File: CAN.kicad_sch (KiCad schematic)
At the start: 32 parts, among them U7 MCP2515-xST, U8 SN65HVD230, Y1 16MHz

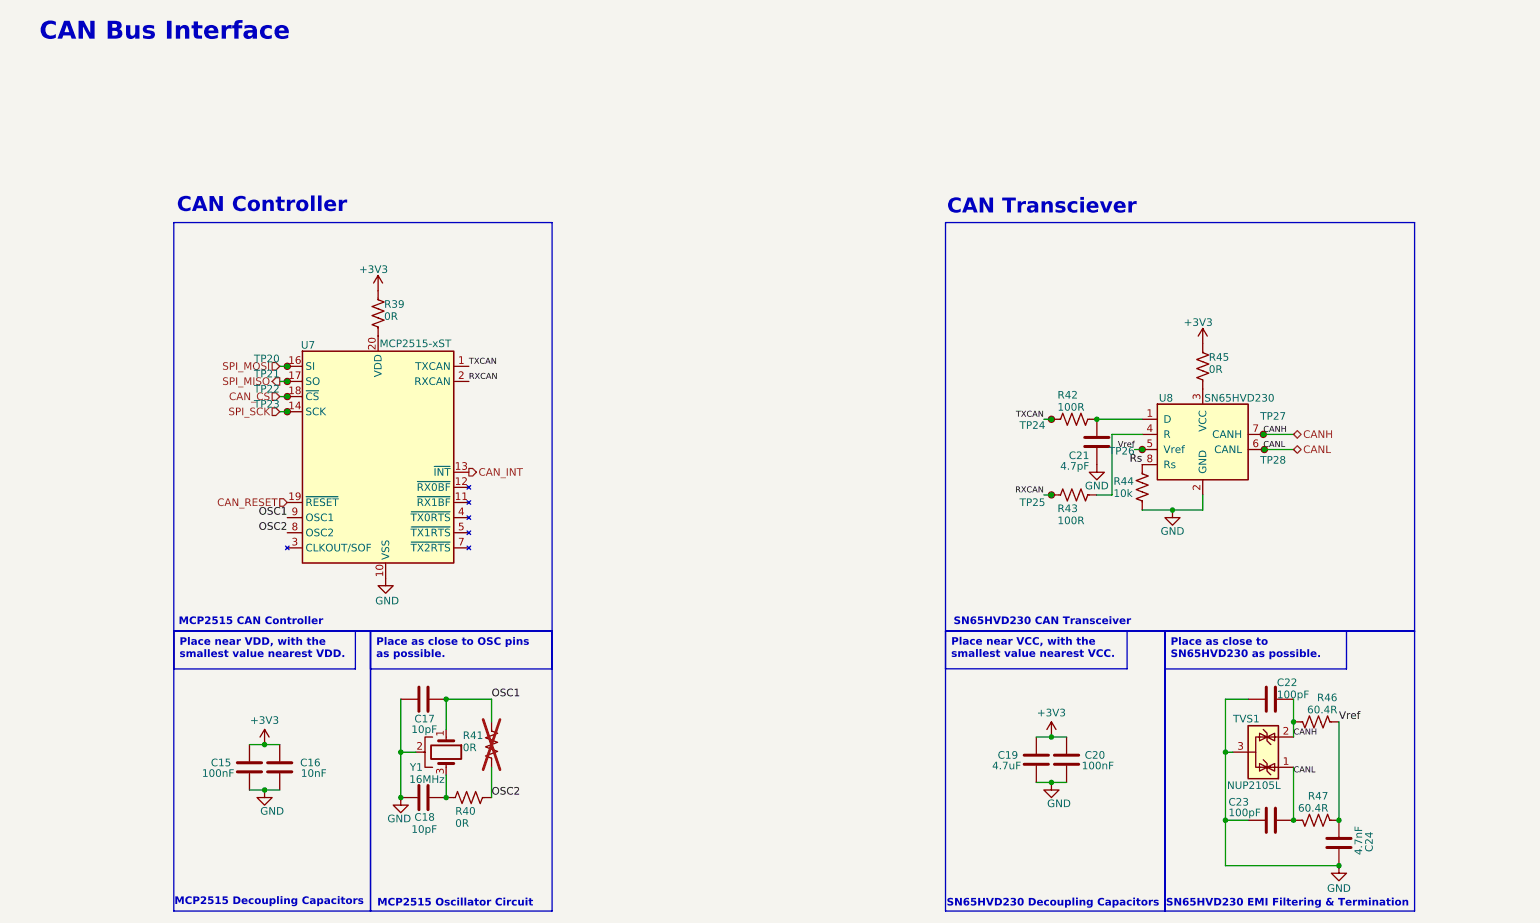
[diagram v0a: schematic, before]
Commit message: Added labels and schematic PDF among other progress
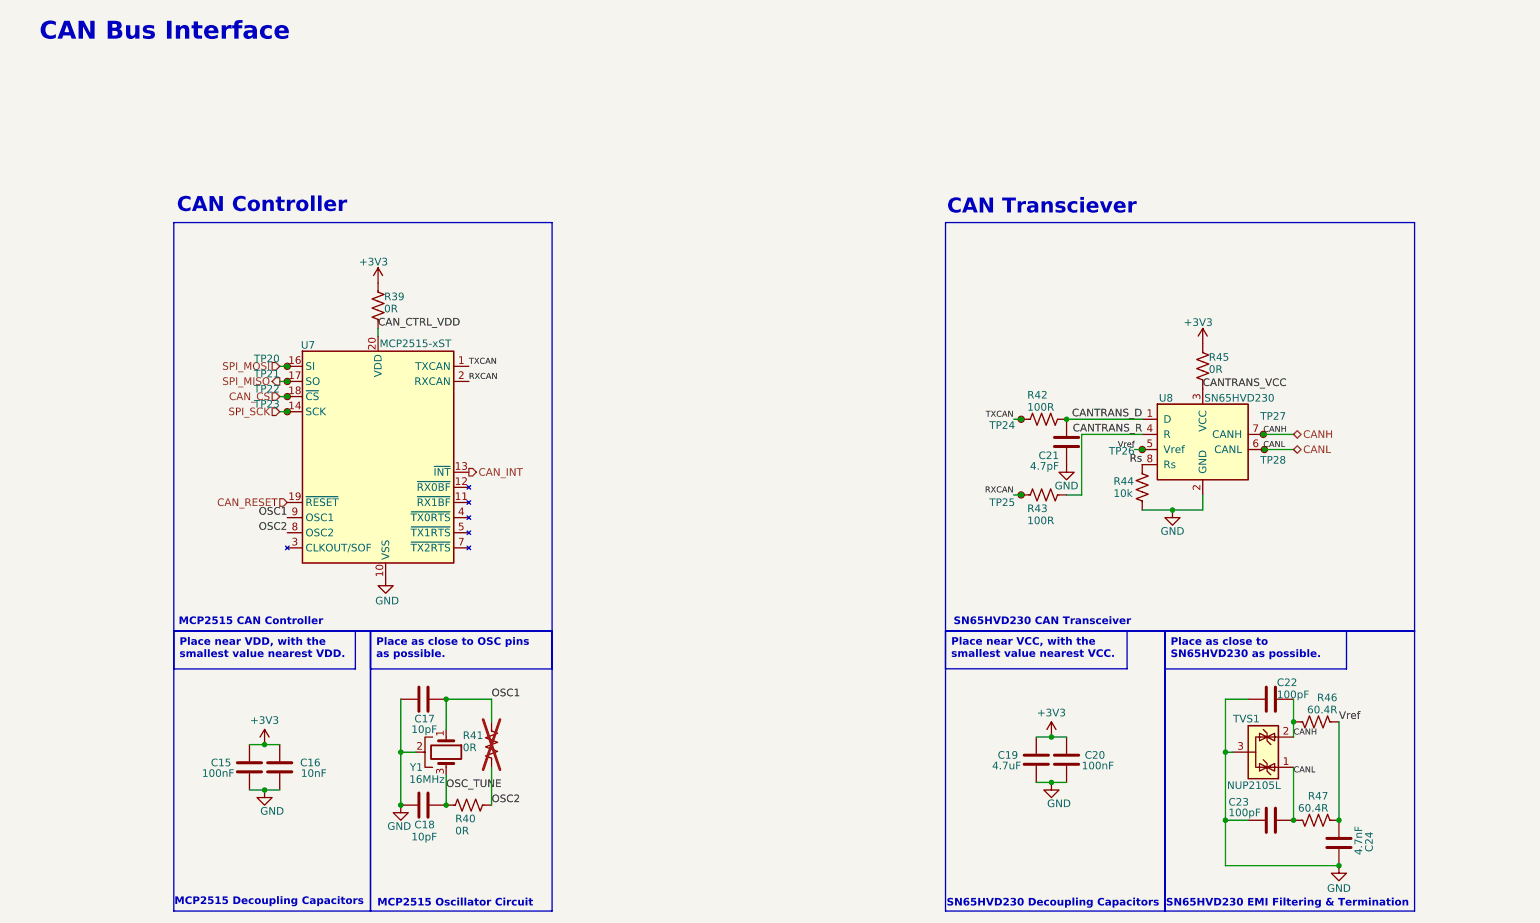
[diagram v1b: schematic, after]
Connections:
- net OSC_TUNE: now reaches C18.2, R40.1, Y1.3
- net CANTRANS_D: now reaches C21.1, R42.2, U8.1 (D)
- net CANTRANS_VCC: now reaches R45.2, U8.3 (VCC)
- net CANTRANS_R: now reaches R43.1, U8.4 (R)
- net CAN_CTRL_VDD: now reaches R39.2, U7.20 (VDD)
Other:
- moved on the sheet: C18, C21, R39, R40, R42, R43, TP24, TP25

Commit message: Added testpoints
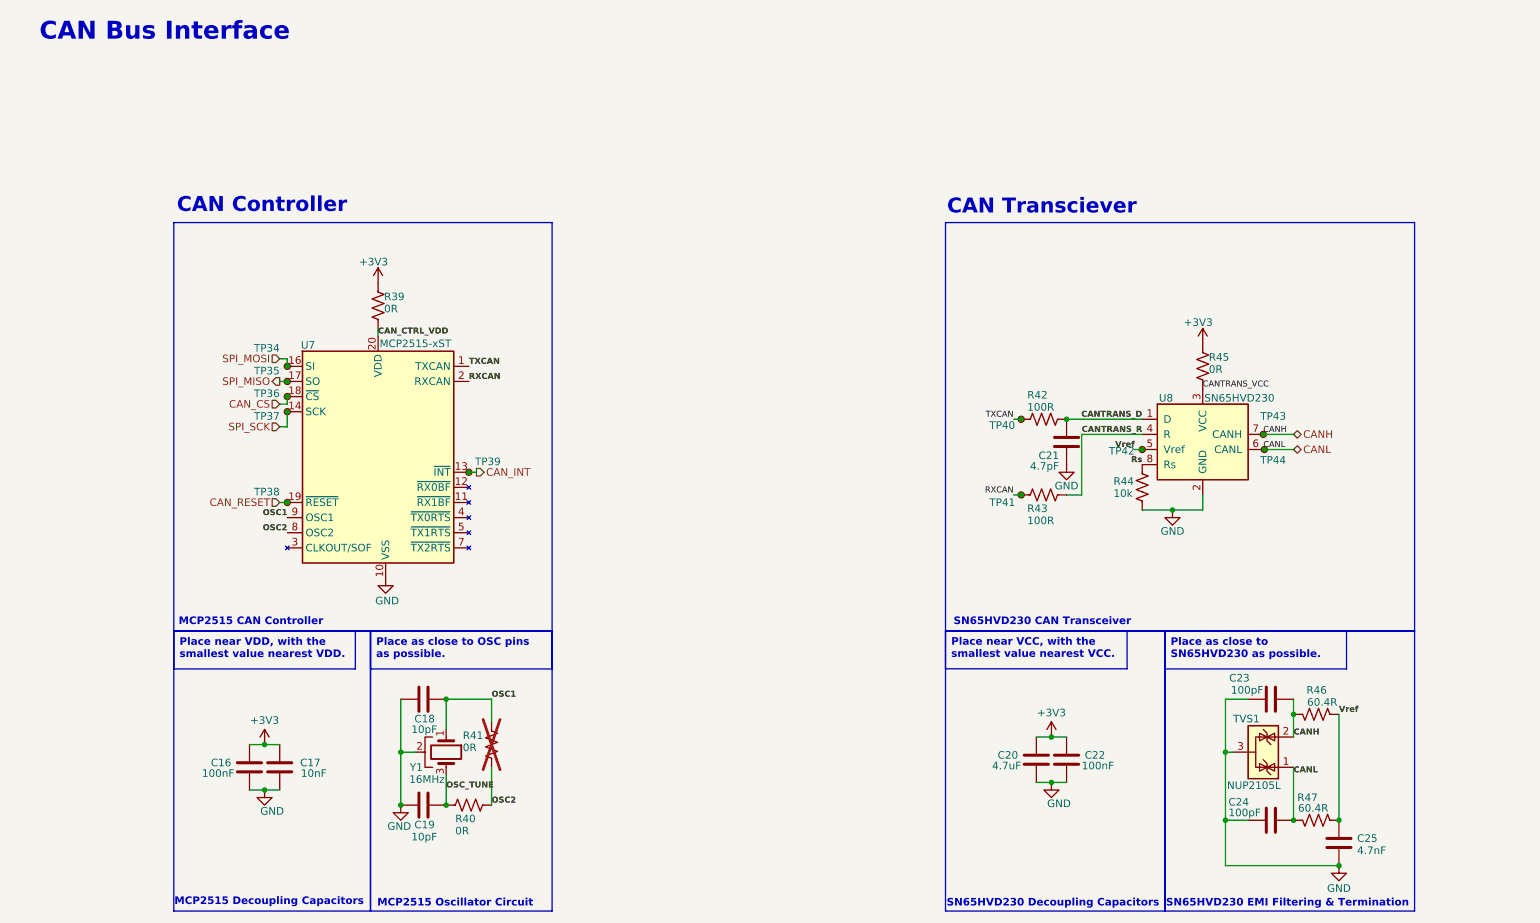
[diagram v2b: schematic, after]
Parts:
- added TP38: CAN_RESET, symbol Connector:TestPoint_Small
- added TP39: CAN_INT, symbol Connector:TestPoint_Small
- renumbered C15 to C16, C16 to C17, C17 to C18, C18 to C19, C19 to C20, C20 to C22, C22 to C23, C23 to C24, C24 to C25, TP20 to TP34, TP21 to TP35, TP22 to TP36, TP23 to TP37, TP24 to TP40, TP25 to TP41, TP26 to TP42, TP27 to TP43, TP28 to TP44
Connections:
- net CANH: now also C23.2; no longer C23.1
- net CAN_INT: now also TP39.1
- net CAN_RESET: now also TP38.1
- net GND: now also C23.1; no longer C23.2
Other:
- moved on the sheet: C23, R46

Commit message: Partially assigned netclasses WIP
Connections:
- net CANTRANS_VCC renamed CAN_TRANS_VCC
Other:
- moved on the sheet: R45
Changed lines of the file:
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@@
 	(wire
 		(pts
+			(xy 69.85 57.15) (xy 69.85 58.42)
+		)
+		(stroke
+			(width 0)
+			(type default)
+		)
+	)
+	(wire
+		(pts
 			(xy 212.09 156.21) (xy 231.14 156.21)
 		)
@@
 	(wire
 		(pts
+			(xy 86.36 74.93) (xy 85.09 74.93)
+		)
+		(stroke
+			(width 0)
+			(type default)
+		)
+	)
+	(wire
+		(pts
 			(xy 53.34 143.51) (xy 50.8 143.51)
 		)
@@
 	(wire
 		(pts
+			(xy 86.36 72.39) (xy 85.09 72.39)
+		)
+		(stroke
+			(width 0)
+			(type default)
+		)
+	)
+	(wire
+		(pts
 			(xy 54.61 78.74) (xy 54.61 77.47)
 		)
@@
 	(wire
 		(pts
+			(xy 208.28 66.04) (xy 208.28 67.31)
+		)
+		(stroke
+			(width 0)
+			(type default)
+		)
+	)
+	(wire
+		(pts
 			(xy 53.34 74.93) (xy 54.61 74.93)
 		)
@@
 	(wire
 		(pts
+			(xy 208.28 74.93) (xy 208.28 76.2)
+		)
+		(stroke
+			(width 0)
+			(type default)
+		)
+	)
+	(wire
+		(pts
 			(xy 50.8 143.51) (xy 48.26 143.51)
 		)
@@
 		)
 	)
-	(label "CANTRANS_VCC"
+	(label "CAN_TRANS_VCC"
 		(at 208.28 76.2 0)
 		(effects
@@
 	)
 	(label "TXCAN"
-		(at 85.09 72.39 0)
+		(at 86.36 72.39 0)
 		(effects
 			(font
@@
 	)
 	(label "RXCAN"
-		(at 85.09 74.93 0)
+		(at 86.36 74.93 0)
 		(effects
 			(font
@@
 	(symbol
 		(lib_id "power:+3V3")
-		(at 208.28 68.58 0)
+		(at 208.28 66.04 0)
 		(unit 1)
 		(body_style 1)
@@
 		(dnp no)
 		(property "Reference" "#PWR052"
-			(at 208.28 72.39 0)
+			(at 208.28 69.85 0)
 			(hide yes)
 			(show_name no)
@@
 		)
 		(property "Value" "+3V3"
-			(at 207.518 65.024 0)
+			(at 207.518 62.484 0)
 			(show_name no)
 			(do_not_autoplace no)
@@
 		)
 		(property "Footprint" ""
-			(at 208.28 68.58 0)
+			(at 208.28 66.04 0)
 			(hide yes)
 			(show_name no)
@@
 		)
 		(property "Datasheet" ""
-			(at 208.28 68.58 0)
+			(at 208.28 66.04 0)
 			(hide yes)
 			(show_name no)
@@
 		)
 		(property "Description" "Power symbol creates a global label with name \"+3V3\""
-			(at 208.28 68.58 0)
+			(at 208.28 66.04 0)
 			(hide yes)
 			(show_name no)
@@
 	(symbol
 		(lib_id "power:+3V3")
-		(at 69.85 58.42 0)
+		(at 69.85 57.15 0)
 		(unit 1)
 		(body_style 1)
@@
 		(dnp no)
 		(property "Reference" "#PWR045"
-			(at 69.85 62.23 0)
+			(at 69.85 60.96 0)
 			(hide yes)
 			(show_name no)
@@
 		)
 		(property "Value" "+3V3"
-			(at 69.088 54.864 0)
+			(at 69.088 53.594 0)
 			(show_name no)
 			(do_not_autoplace no)
@@
 		)
 		(property "Footprint" ""
-			(at 69.85 58.42 0)
+			(at 69.85 57.15 0)
 			(hide yes)
 			(show_name no)
@@
 		)
 		(property "Datasheet" ""
-			(at 69.85 58.42 0)
+			(at 69.85 57.15 0)
 			(hide yes)
 			(show_name no)
@@
 		)
 		(property "Description" "Power symbol creates a global label with name \"+3V3\""
-			(at 69.85 58.42 0)
+			(at 69.85 57.15 0)
 			(hide yes)
 			(show_name no)
@@
 	(symbol
 		(lib_id "Device:R_US")
-		(at 208.28 72.39 0)
+		(at 208.28 71.12 0)
 		(unit 1)
 		(body_style 1)
@@
 		(dnp no)
 		(property "Reference" "R45"
-			(at 209.296 70.866 0)
+			(at 209.296 69.596 0)
 			(show_name no)
 			(do_not_autoplace no)
@@
 		)
 		(property "Value" "0R"
-			(at 209.296 72.898 0)
+			(at 209.296 71.628 0)
 			(show_name no)
 			(do_not_autoplace no)
@@
 		)
 		(property "Footprint" "Resistor_SMD:R_0805_2012Metric"
-			(at 209.296 72.644 90)
+			(at 209.296 71.374 90)
 			(hide yes)
 			(show_name no)
@@
 		)
 		(property "Datasheet" ""
-			(at 208.28 72.39 0)
+			(at 208.28 71.12 0)
 			(hide yes)
 			(show_name no)
@@
 		)
 		(property "Description" "Resistor, US symbol"
-			(at 208.28 72.39 0)
+			(at 208.28 71.12 0)
 			(hide yes)
 			(show_name no)
@@
 		)
 		(property "MFR#" ""
-			(at 208.28 72.39 0)
+			(at 208.28 71.12 0)
 			(hide yes)
 			(show_name no)
@@
 		)
 		(property "Package" "0805"
-			(at 208.28 72.39 0)
+			(at 208.28 71.12 0)
 			(hide yes)
 			(show_name no)
@@
 		)
 		(property "LCSC#" "C54921246"
-			(at 208.28 72.39 0)
+			(at 208.28 71.12 0)
 			(hide yes)
 			(show_name no)

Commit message: Configured Varients
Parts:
- renumbered R39 to R40, R40 to R41, R41 to R42, R42 to R43, R43 to R44, R44 to R45, R45 to R46, R46 to R47, R47 to R48
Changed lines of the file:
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@@
 					(reference "C20")
 					(unit 1)
+					(variant
+						(name "5v Dumb")
+						(dnp yes)
+					)
 				)
 			)
@@
 		(in_pos_files yes)
 		(dnp no)
-		(property "Reference" "R44"
+		(property "Reference" "R45"
 			(at 193.294 91.694 0)
 			(show_name no)
@@
 			(project "power_module"
 				(path "/33e2b92e-f705-4be7-96f4-57092b8ec1ea/2c777b8c-fce7-4c8f-b22a-e5c1ebb4dbeb"
-					(reference "R44")
+					(reference "R45")
 					(unit 1)
+					(variant
+						(name "5v Dumb")
+						(dnp yes)
+					)
 				)
 			)
@@
 					(reference "C19")
 					(unit 1)
+					(variant
+						(name "5v Dumb")
+						(dnp yes)
+					)
 				)
 			)
@@
 					(reference "C25")
 					(unit 1)
+					(variant
+						(name "5v Dumb")
+						(dnp yes)
+					)
 				)
 			)
@@
 					(reference "U8")
 					(unit 1)
+					(variant
+						(name "5v Dumb")
+						(dnp yes)
+					)
 				)
 			)
@@
 					(reference "C22")
 					(unit 1)
+					(variant
+						(name "5v Dumb")
+						(dnp yes)
+					)
 				)
 			)
@@
 					(reference "Y1")
 					(unit 1)
+					(variant
+						(name "5v Dumb")
+						(dnp yes)
+					)
 				)
 			)
@@
 					(reference "C17")
 					(unit 1)
+					(variant
+						(name "5v Dumb")
+						(dnp yes)
+					)
 				)
 			)
@@
 		(in_pos_files yes)
 		(dnp no)
-		(property "Reference" "R47"
+		(property "Reference" "R48"
 			(at 227.584 144.78 90)
 			(show_name no)
@@
 			(project "power_module"
 				(path "/33e2b92e-f705-4be7-96f4-57092b8ec1ea/2c777b8c-fce7-4c8f-b22a-e5c1ebb4dbeb"
-					(reference "R47")
+					(reference "R48")
 					(unit 1)
+					(variant
+						(name "5v Dumb")
+						(dnp yes)
+					)
 				)
 			)
@@
 		(in_pos_files yes)
 		(dnp yes)
-		(property "Reference" "R41"
+		(property "Reference" "R42"
 			(at 84.074 134.366 0)
 			(show_name no)
@@
 			(project "power_module"
 				(path "/33e2b92e-f705-4be7-96f4-57092b8ec1ea/2c777b8c-fce7-4c8f-b22a-e5c1ebb4dbeb"
-					(reference "R41")
+					(reference "R42")
 					(unit 1)
 				)
@@
 					(reference "C24")
 					(unit 1)
+					(variant
+						(name "5v Dumb")
+						(dnp yes)
+					)
 				)
 			)
@@
 		(in_pos_files yes)
 		(dnp no)
-		(property "Reference" "R42"
+		(property "Reference" "R43"
 			(at 178.816 77.216 90)
 			(show_name no)
@@
 			(project "power_module"
 				(path "/33e2b92e-f705-4be7-96f4-57092b8ec1ea/2c777b8c-fce7-4c8f-b22a-e5c1ebb4dbeb"
-					(reference "R42")
+					(reference "R43")
 					(unit 1)
+					(variant
+						(name "5v Dumb")
+						(dnp yes)
+					)
 				)
 			)
@@
 		(in_pos_files yes)
 		(dnp no)
-		(property "Reference" "R45"
+		(property "Reference" "R46"
 			(at 209.296 69.596 0)
 			(show_name no)
@@
 			(project "power_module"
 				(path "/33e2b92e-f705-4be7-96f4-57092b8ec1ea/2c777b8c-fce7-4c8f-b22a-e5c1ebb4dbeb"
-					(reference "R45")
+					(reference "R46")
 					(unit 1)
+					(variant
+						(name "5v Dumb")
+						(dnp yes)
+					)
 				)
 			)
@@
 					(reference "C21")
 					(unit 1)
+					(variant
+						(name "5v Dumb")
+						(dnp yes)
+					)
 				)
 			)
@@
 		(in_pos_files yes)
 		(dnp no)
-		(property "Reference" "R40"
+		(property "Reference" "R41"
 			(at 82.804 148.336 90)
 			(show_name no)
@@
 			(project "power_module"
 				(path "/33e2b92e-f705-4be7-96f4-57092b8ec1ea/2c777b8c-fce7-4c8f-b22a-e5c1ebb4dbeb"
-					(reference "R40")
+					(reference "R41")
 					(unit 1)
+					(variant
+						(name "5v Dumb")
+						(dnp yes)
+					)
 				)
 			)
@@
 					(reference "C16")
 					(unit 1)
+					(variant
+						(name "5v Dumb")
+						(dnp yes)
+					)
 				)
 			)
@@
 		(in_pos_files yes)
 		(dnp no)
-		(property "Reference" "R39"
+		(property "Reference" "R40"
 			(at 70.866 60.706 0)
 			(show_name no)
@@
 			(project "power_module"
 				(path "/33e2b92e-f705-4be7-96f4-57092b8ec1ea/2c777b8c-fce7-4c8f-b22a-e5c1ebb4dbeb"
-					(reference "R39")
+					(reference "R40")
 					(unit 1)
+					(variant
+						(name "5v Dumb")
+						(dnp yes)
+					)
 				)
 			)
@@
 					(reference "C23")
 					(unit 1)
+					(variant
+						(name "5v Dumb")
+						(dnp yes)
+					)
 				)
 			)
@@
 		(in_pos_files yes)
 		(dnp no)
-		(property "Reference" "R43"
+		(property "Reference" "R44"
 			(at 178.816 96.266 90)
 			(show_name no)
@@
 			(project "power_module"
 				(path "/33e2b92e-f705-4be7-96f4-57092b8ec1ea/2c777b8c-fce7-4c8f-b22a-e5c1ebb4dbeb"
-					(reference "R43")
+					(reference "R44")
 					(unit 1)
+					(variant
+						(name "5v Dumb")
+						(dnp yes)
+					)
 				)
 			)
@@
 					(reference "TVS1")
 					(unit 1)
+					(variant
+						(name "5v Dumb")
+						(dnp yes)
+					)
 				)
 			)
@@
 					(reference "U7")
 					(unit 1)
+					(variant
+						(name "5v Dumb")
+						(dnp yes)
+					)
 				)
 			)
@@
 		(in_pos_files yes)
 		(dnp no)
-		(property "Reference" "R46"
+		(property "Reference" "R47"
 			(at 229.108 126.746 90)
 			(show_name no)
@@
 			(project "power_module"
 				(path "/33e2b92e-f705-4be7-96f4-57092b8ec1ea/2c777b8c-fce7-4c8f-b22a-e5c1ebb4dbeb"
-					(reference "R46")
+					(reference "R47")
 					(unit 1)
+					(variant
+						(name "5v Dumb")
+						(dnp yes)
+					)
 				)
 			)
@@
 					(reference "C18")
 					(unit 1)
+					(variant
+						(name "5v Dumb")
+						(dnp yes)
+					)
 				)
 			)
